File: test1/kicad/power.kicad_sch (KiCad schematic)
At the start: 0 parts

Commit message: test1: fill in Power, Bias, Bobcat, Connectors, FMC sheets
Completes the test1 Bobcat carrier hierarchical schematic. All 7 sheets
(root + 6 children) parse cleanly with kicad-cli and render to SVG/PDF.

Contents per child:
  - power.kicad_sch       — TPS7A8401A LDO (3P3V → 0.8V via ANY-OUT
                            strap, OUT side fans to +VDDD/+VDDA1/+VDDA2
                            via 1×2 jumpers) + TPS22916 load switch
                            (VADJ → +VDDIO) with EN pulldowns + decoupling.
  - bobcat.kicad_sch      — Bobcat 40-QFN DUT with VDDD/VDDIO decoupling,
                            VDDA1/VDDA2 series 0Ω + decoupling, hier-label
                            exits on all four edges for SAMPLE_OUT*,
                            SPI, GPIO, CLK_OUT*, BIAS0/1, etc.
  - eeprom.kicad_sch      — 24AA08 I²C EEPROM (address 000, WP→GND,
                            0.1 µF decoupling, 2.2 kΩ I²C pull-ups).
  - bias.kicad_sch        — MCP4728 quad DAC + OPA2388 dual op-amp
                            (units 1 & 2) + PMZ1200UPEYL high-side PMOS
                            × 2 channels + 5.11 kΩ 0.1% sense resistors +
                            DNP 2N7002 isolation NMOS placeholders.
  - connectors.kicad_sch  — 4× SMA for CLK_OUT0–3, 3× SMA for
                            OSC_EN/WEIGHT_EN/SAMPLE_TRIG, 1×4 GPIO
                            header, 3× Keystone-5011 GND test clips.
  - fmc.kicad_sch         — VITA 57.1 LPC connector (4 units × 40 pins),
                            wired for 3P3V/VADJ/SCL/SDA/PRSNT/GA0/GA1/
                            PG_C2M/LDO_EN/LSW_EN; LA-bank pins NC'd for
                            later pinning; all other C/D/G/H pins to GND.

Generator improvements driven by this round:
  - Multi-unit symbol support (parse_pins now returns the per-pin unit
    number; place() takes a unit= parameter and emits matching (unit N)
    in the instance + path).
  - Escape backslash/quote in property values so refs/values with
    embedded " (e.g. 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
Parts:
- added C1: 10uF, Capacitor_SMD:C_0805_2012Metric, symbol Device:C
- added C2, C5, C6, C7: 0.1uF, Capacitor_SMD:C_0402_1005Metric, symbol Device:C
- added C3: 10nF, Capacitor_SMD:C_0402_1005Metric, symbol Device:C
- added C4: 22uF, Capacitor_SMD:C_0805_2012Metric, symbol Device:C
- added J1, J2, J3: 1x2 100mil, Connector_PinHeader_2.54mm:PinHeader_1x02_P2.54mm_Vertical, symbol Lib:TSW-102-05-G-S
- added R1, R2: 10k, Resistor_SMD:R_0402_1005Metric, symbol Device:R
- added U1: TPS7A8401A, Package_DFN_QFN:VQFN-20-1EP_3.5x3.5mm_P0.5mm_EP1.6x1.6mm, symbol Lib:TPS7A8401A
- added U2: TPS22916, Package_DirectFETandLGA:Texas_DSBGA-4_0.6x1.0mm_Layout2x2_P0.4mm, symbol Lib:TPS22916CNYFPR
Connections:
- new net: C4.1, C5.1, J1.1, J2.1, J3.1, U1.1 (OUT), U1.2 (SNS), U1.20 (OUT), U1.3 (FB)
- new net +3V3: C1.1, C2.1, U1.12 (BIAS), U1.15 (IN), U1.16 (IN), U1.17 (IN)
- new net +VDDA1: J2.2
- new net +VDDA2: J3.2
- new net +VDDD: J1.2
- new net +VDDIO: C7.1, U2.A1 (VOUT)
- new net GND: C1.2, C2.2, C3.1, C3.2, C4.2, C5.2, C6.2, C7.2, R1.2, R2.2, U1.13 (NR_SS), U1.18 (GND), U1.21 (PAD), U1.6 (100_mV), U1.7 (200_mV), U1.8 (GND), U2.B1 (GND)
- new net LDO_EN: R1.1, U1.14 (EN)
- new net LDO_PG: U1.4 (PG)
- new net LSW_EN: R2.1, U2.B2 (ON)
- new net VADJ: C6.1, U2.A2 (VIN)
- no-connect marks 0 -> 4
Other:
- title: test1 — Power -> test1 — Power (LDO + Load Switch)

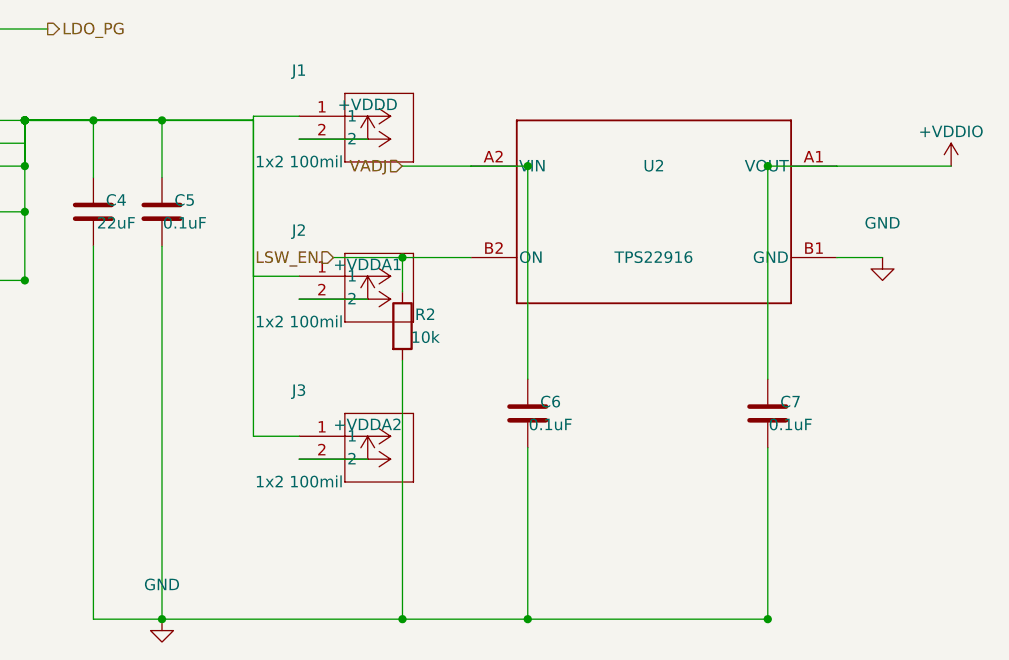
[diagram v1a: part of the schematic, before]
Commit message: Apply layout best-practices from reference schematic
Skill updates (from the LTC3114 reference sample):
  - New rule 5: no net passes through a component body (visual ambiguity).
  - New rule 6: every placed component is in-path or removed — DNP parts
    stay wired in series and just carry (dnp yes) + "DNP" value tag; never
    leave a part with no_connect on all its pins as a "for later"
    placeholder.
  - New rule 7: GND symbols cluster — one (power:GND) per local pin group,
    not one per pin. Connector banks bus their GNDs onto a single rail
    with one terminating triangle.
  - New rule 8: canonical decoupling-cap cluster (bulk+HF share one rail
    above and one GND below; stay off the path of unrelated nets).

test1 design fixes (each addresses a specific point raised on review):

  1. Bias: Q3, Q4 (2N7002 NMOS isolators) now wired in series between
     each PMOS drain and the BIASx output — gates exit as BIAS_ISO0 /
     BIAS_ISO1 hier labels for MCU control. Marked DNP via "2N7002 DNP"
     value. No more orphaned no_connects.

  2. Bobcat: VDDA2 decoupling cap C4 moved onto its own branch BELOW the
     R6 series-0Ω lane, off the pin-26/27 tie wire path.

  3. FMC: ~150 individual per-pin GND symbols collapsed into one
     consolidated GND rail per unit (J1/J2/J3/J4), each terminating in a
     single GND triangle at the rail's bottom.

  4. Power: TPS22916 (U2) decoupling caps C6 and C7 moved ALONGSIDE the
     chip body (left and right) at the same y as VIN/VOUT — wires no
     longer pass under the chip footprint. Cap pin 1 (top) → chip pin
     via horizontal stub; cap pin 2 (bot) → GND rail below.

Co-Authored-By: Claude Opus 4.7 (1M context) <noreply@anthropic.com>
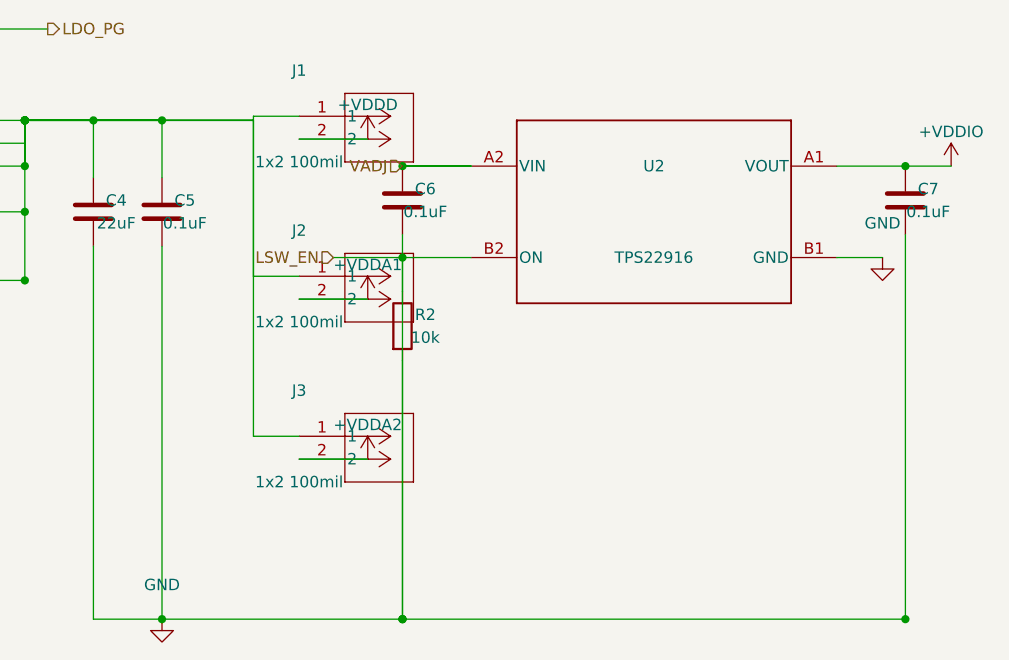
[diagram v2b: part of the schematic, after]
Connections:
- net LSW_EN is gone; now on net GND: R2.1, U2.B2 (ON)
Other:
- moved on the sheet: C6, C7
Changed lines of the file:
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@@
   (symbol
     (lib_id "Device:C")
-    (at 220.98 152.4 0)
+    (at 207.06 128.73 0)
     (unit 1) (in_bom yes) (on_board yes) (dnp no)
-    (property "Reference" "C6" (at 223.51999999999998 151.13 0) (effects (font (size 1.27 1.27))))
-    (property "Value" "0.1uF" (at 223.51999999999998 153.67000000000002 0) (effects (font (size 1.27 1.27))))
+    (property "Reference" "C6" (at 209.6 127.46 0) (effects (font (size 1.27 1.27))))
+    (property "Value" "0.1uF" (at 209.6 130.0 0) (effects (font (size 1.27 1.27))))
     (property "Footprint" "Capacitor_SMD:C_0402_1005Metric" (at 0 0 0) (effects (font (size 1.27 1.27)) (hide yes)))
     (property "Datasheet" "" (at 0 0 0) (effects (font (size 1.27 1.27)) (hide yes)))
@@
       (project "test1"
         (path "/4ed7a046-ef33-57d9-8730-321c05965af3/45af8917-b3aa-56de-8c9b-8d649d910e5f" (reference "C6") (unit 1)))))
-  (wire (pts (xy 220.98 148.59) (xy 220.98 124.92)) (stroke (width 0) (type default)))
-  (wire (pts (xy 220.98 124.92) (xy 214.68 124.92)) (stroke (width 0) (type default)))
-  (junction (at 220.98 124.92) (diameter 0) (color 0 0 0 0))
-  (wire (pts (xy 220.98 156.21) (xy 220.98 175.26)) (stroke (width 0) (type default)))
-  (wire (pts (xy 180.34 175.26) (xy 220.98 175.26)) (stroke (width 0) (type default)))
-  (junction (at 220.98 175.26) (diameter 0) (color 0 0 0 0))
+  (wire (pts (xy 207.06 124.92) (xy 214.68 124.92)) (stroke (width 0) (type default)))
+  (junction (at 207.06 124.92) (diameter 0) (color 0 0 0 0))
+  (wire (pts (xy 207.06 132.54) (xy 207.06 175.26)) (stroke (width 0) (type default)))
+  (wire (pts (xy 207.06 175.26) (xy 180.34 175.26)) (stroke (width 0) (type default)))
+  (junction (at 207.06 175.26) (diameter 0) (color 0 0 0 0))
   (symbol
     (lib_id "Device:C")
-    (at 247.65 152.4 0)
+    (at 262.94 128.73 0)
     (unit 1) (in_bom yes) (on_board yes) (dnp no)
-    (property "Reference" "C7" (at 250.19 151.13 0) (effects (font (size 1.27 1.27))))
-    (property "Value" "0.1uF" (at 250.19 153.67000000000002 0) (effects (font (size 1.27 1.27))))
+    (property "Reference" "C7" (at 265.48 127.46 0) (effects (font (size 1.27 1.27))))
+    (property "Value" "0.1uF" (at 265.48 130.0 0) (effects (font (size 1.27 1.27))))
     (property "Footprint" "Capacitor_SMD:C_0402_1005Metric" (at 0 0 0) (effects (font (size 1.27 1.27)) (hide yes)))
     (property "Datasheet" "" (at 0 0 0) (effects (font (size 1.27 1.27)) (hide yes)))
@@
       (project "test1"
         (path "/4ed7a046-ef33-57d9-8730-321c05965af3/45af8917-b3aa-56de-8c9b-8d649d910e5f" (reference "C7") (unit 1)))))
-  (wire (pts (xy 247.65 148.59) (xy 247.65 124.92)) (stroke (width 0) (type default)))
-  (wire (pts (xy 247.65 124.92) (xy 255.32 124.92)) (stroke (width 0) (type default)))
-  (junction (at 247.65 124.92) (diameter 0) (color 0 0 0 0))
-  (wire (pts (xy 247.65 156.21) (xy 247.65 175.26)) (stroke (width 0) (type default)))
-  (wire (pts (xy 220.98 175.26) (xy 247.65 175.26)) (stroke (width 0) (type default)))
-  (junction (at 247.65 175.26) (diameter 0) (color 0 0 0 0))
+  (wire (pts (xy 262.94 124.92) (xy 262.94 124.92)) (stroke (width 0) (type default)))
+  (junction (at 262.94 124.92) (diameter 0) (color 0 0 0 0))
+  (wire (pts (xy 262.94 132.54) (xy 262.94 175.26)) (stroke (width 0) (type default)))
+  (wire (pts (xy 207.06 175.26) (xy 262.94 175.26)) (stroke (width 0) (type default)))
+  (junction (at 262.94 175.26) (diameter 0) (color 0 0 0 0))
   (symbol
     (lib_id "Device:R")
